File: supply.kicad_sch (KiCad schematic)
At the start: 126 parts, among them IC1 TPS54561QDPRRQ1, IC2 TPS54561QDPRRQ1, J1 BarrelJack_3167288, J2 PinHeader_1x3_P2.54mm_Drill1.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, U1 AP62301WU-7, U2 AP62301WU-7, U3 AP62301WU-7, U4 AP62301WU-7, U5 AP62301WU-7, U6 LM3881MME_NOPB

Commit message: [#65754] Rev 2.0.0 Initial commit - source design files from so-dimm-ddr5-tester e0a54f86
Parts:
- removed 1V0, 1V1, 1V8, 3V3, GND1, TP1, TP2, TP3, TP4: TP_1mm_SMD, antmicro-footprints:TP_SMD_1mm, symbol data-center-rdimm-ddr5-tester:TP_1mm_SMD
- removed C1, C2, C3, C4, C5, C6: C_47u_16V_1206, data-center-rdimm-ddr5-tester-footprints:C_1206_3216Metric, symbol data-center-rdimm-ddr5-tester:C_47u_16V_1206
- removed C10, C12: C_47p_0402, data-center-rdimm-ddr5-tester-footprints:C_0402_1005Metric, symbol data-center-rdimm-ddr5-tester:C_47p_0402
- removed C11, C9: C_10n_0402, data-center-rdimm-ddr5-tester-footprints:C_0402_1005Metric, symbol data-center-rdimm-ddr5-tester:C_10n_0402
- removed C13, C14, C26, C27, C28, C29, C30, C42: C_100n_6V3_0402, data-center-rdimm-ddr5-tester-footprints:C_0402_1005Metric, symbol data-center-rdimm-ddr5-tester:C_100n_6V3_0402
- removed C15, C16, C17, C18, C19, C20: C_47u_0603, data-center-rdimm-ddr5-tester-footprints:C_0603_1608Metric, symbol data-center-rdimm-ddr5-tester:C_47u_0603
- removed C177, C178, C179, C180, C181: C_1u_0402, data-center-rdimm-ddr5-tester-footprints:C_0402_1005Metric, symbol data-center-rdimm-ddr5-tester:C_1u_0402
- removed C21, C22, C23, C24, C25: C_10u_0402, data-center-rdimm-ddr5-tester-footprints:C_0402_1005Metric, symbol data-center-rdimm-ddr5-tester:C_10u_0402
- removed C31, C32, C33, C34, C35, C36, C37, C38, C39, C40: C_22u_0402, data-center-rdimm-ddr5-tester-footprints:C_0402_1005Metric, symbol data-center-rdimm-ddr5-tester:C_22u_0402
- removed C41: C_10n_0603, data-center-rdimm-ddr5-tester-footprints:C_0603_1608Metric, symbol data-center-rdimm-ddr5-tester:C_10n_0603
- removed C7, C8: C_4n7_0402, data-center-rdimm-ddr5-tester-footprints:C_0402_1005Metric, symbol data-center-rdimm-ddr5-tester:C_4n7_0402
- removed D1, D2, D3: PDS760, data-center-rdimm-ddr5-tester-footprints:PowerDI5, symbol data-center-rdimm-ddr5-tester:PDS760
- removed F1, F2, F3, F4, F5, F6, F7: PTC_4.5A_1206, data-center-rdimm-ddr5-tester-footprints:F_1206_3216Metric, symbol data-center-rdimm-ddr5-tester:PTC_4.5A_1206
- removed IC1, IC2: TPS54561QDPRRQ1, data-center-rdimm-ddr5-tester-footprints:WSON-10-1EP_4x4mm_P0.8mm_EP2.6x3mm, symbol data-center-rdimm-ddr5-tester:TPS54561QDPRRQ1
- removed J1: BarrelJack_3167288, data-center-rdimm-ddr5-tester-footprints:BarrelJack_3167288_Horizontal, symbol data-center-rdimm-ddr5-tester:BarrelJack_3167288
- removed J2: PinHeader_1x3_P2.54mm_Drill1.1mm, data-center-rdimm-ddr5-tester-footprints:PinHeader_1x3_P2.54mm_Drill1.1mm, symbol data-center-rdimm-ddr5-tester:PinHeader_1x3_P2.54mm_Drill1.1mm
- removed L1, L2: L_7u2_7.9A_WE-PDF, data-center-rdimm-ddr5-tester-footprints:L_WE-PDF, symbol data-center-rdimm-ddr5-tester:L_7u2_7.9A_WE-PDF
- removed L3, L5, L6, L7, L8: L_1u5_6A_1716, data-center-rdimm-ddr5-tester-footprints:L_1716_4441Metric, symbol data-center-rdimm-ddr5-tester:L_1u5_6A_1716
- removed POT1: TC33X-2-203E, data-center-rdimm-ddr5-tester-footprints:Trimpot_3.8mmx3.6mm_TC33X-2-103E, symbol data-center-rdimm-ddr5-tester:TC33X-2-203E
- removed PWR1: LED_G_0603_KP-1608CGCK, data-center-rdimm-ddr5-tester-footprints:LED_0603_1608Metric_G, symbol data-center-rdimm-ddr5-tester:LED_G_0603_KP-1608CGCK
- removed R1, R142, R16, R17, R18, R19, R20, R31: R_0R_0402, data-center-rdimm-ddr5-tester-footprints:R_0402_1005Metric, symbol data-center-rdimm-ddr5-tester:R_0R_0402
- removed R10: R_43k_0402, data-center-rdimm-ddr5-tester-footprints:R_0402_1005Metric, symbol data-center-rdimm-ddr5-tester:R_43k_0402
- removed R11, R8, R9: R_100k_0402, data-center-rdimm-ddr5-tester-footprints:R_0402_1005Metric, symbol data-center-rdimm-ddr5-tester:R_100k_0402
- removed R12, R15: R_10k2_0402, data-center-rdimm-ddr5-tester-footprints:R_0402_1005Metric, symbol data-center-rdimm-ddr5-tester:R_10k2_0402
- removed R13: R_49R9_0402, data-center-rdimm-ddr5-tester-footprints:R_0402_1005Metric, symbol data-center-rdimm-ddr5-tester:R_49R9_0402
- removed R14: R_53k6_0402, data-center-rdimm-ddr5-tester-footprints:R_0402_1005Metric, symbol data-center-rdimm-ddr5-tester:R_53k6_0402
- removed R141, R24, R28, R30, R32, R33, R34: R_10k_0402, data-center-rdimm-ddr5-tester-footprints:R_0402_1005Metric, symbol data-center-rdimm-ddr5-tester:R_10k_0402
- removed R143, R4, R5: R_243k_0402, data-center-rdimm-ddr5-tester-footprints:R_0402_1005Metric, symbol data-center-rdimm-ddr5-tester:R_243k_0402
- removed R2, R3: R_16k9_0402, data-center-rdimm-ddr5-tester-footprints:R_0402_1005Metric, symbol data-center-rdimm-ddr5-tester:R_16k9_0402
- removed R21: R_1k5_0402, data-center-rdimm-ddr5-tester-footprints:R_0402_1005Metric, symbol data-center-rdimm-ddr5-tester:R_1k5_0402
- removed R22: R_1k_0402, data-center-rdimm-ddr5-tester-footprints:R_0402_1005Metric, symbol data-center-rdimm-ddr5-tester:R_1k_0402
- removed R23: R_12k4_0402, data-center-rdimm-ddr5-tester-footprints:R_0402_1005Metric, symbol data-center-rdimm-ddr5-tester:R_12k4_0402
- removed R25: R_7k5_0402, data-center-rdimm-ddr5-tester-footprints:R_0402_1005Metric, symbol data-center-rdimm-ddr5-tester:R_7k5_0402
- removed R26: R_20k_0402, data-center-rdimm-ddr5-tester-footprints:R_0402_1005Metric, symbol data-center-rdimm-ddr5-tester:R_20k_0402
- removed R27: R_31k6_0402, data-center-rdimm-ddr5-tester-footprints:R_0402_1005Metric, symbol data-center-rdimm-ddr5-tester:R_31k6_0402
- removed R29: R_4k99_0402, data-center-rdimm-ddr5-tester-footprints:R_0402_1005Metric, symbol data-center-rdimm-ddr5-tester:R_4k99_0402
- removed R6: R_0R_2010, data-center-rdimm-ddr5-tester-footprints:R_2010_5025Metric, symbol data-center-rdimm-ddr5-tester:R_0R_2010
- removed R7: R_330R_0402, data-center-rdimm-ddr5-tester-footprints:R_0402_1005Metric, symbol data-center-rdimm-ddr5-tester:R_330R_0402
- removed S1: SW_EG1218, data-center-rdimm-ddr5-tester-footprints:SW_Slide_E-Switch_EG1218, symbol data-center-rdimm-ddr5-tester:SW_EG1218
- removed U1, U2, U3, U4, U5: AP62301WU-7, antmicro-footprints:TSOT23-6, symbol data-center-rdimm-ddr5-tester:AP62301_TSOT
- removed U6: LM3881MME_NOPB, data-center-rdimm-ddr5-tester-footprints:VSSOP-8_3x3mm_P0.65mm, symbol data-center-rdimm-ddr5-tester:LM3881
- added C169, C170, C175, C176, C195, C199, C203, C204, C205, C208, C209, C212, C214, C216, C220: C_100n_0402, antmicro-footprints:C_0402_1005Metric, symbol antmicroCapacitors0402:C_100n_0402
- added C171, C173, C177, C178, C200, C202: C_22u_25V_0805, antmicro-footprints:C_0805_2012Metric, symbol antmicroCapacitorsmisc:C_22u_25V_0805
- added C172, C174, C194, C198, C206: C_1u_0402, antmicro-footprints:C_0402_1005Metric, symbol antmicroCapacitors0402:C_1u_0402
- added C179, C180, C181: C_1u_25V_0603, antmicro-footprints:C_0603_1608Metric, symbol antmicroCapacitors0603:C_1u_25V_0603
- added C182, C183, C184, C185, C186, C187, C188, C189, C190, C191, C192, C193, C213, C215, C217, C219: C_22u_0603, antmicro-footprints:C_0603_1608Metric, symbol antmicroCapacitors0603:C_22u_0603
- added C201: C_470n_0402, antmicro-footprints:C_0402_1005Metric, symbol antmicroCapacitors0402:C_470n_0402
- added C207, C211, C218: C_10u_6.3V_0402, antmicro-footprints:C_0402_1005Metric, symbol antmicroCapacitors0402:C_10u_6.3V_0402
- added C210: C_22n_0402, antmicro-footprints:C_0402_1005Metric, symbol antmicroCapacitors0402:C_22n_0402
- added C221: C_22p_0402, antmicro-footprints:C_0402_1005Metric, symbol antmicroCapacitors0402:C_22p_0402
- added D16: ESDA25P35-1U1M, antmicro-footprints:ESDA25P35-1U1M, symbol antmicroTVSDiodes:ESDA25P35-1U1M
- added F1, F2: F_4A_1206, antmicro-footprints:F_1206_3216Metric, symbol antmicroFuses:F_4A_1206
- added J7: BarrelJack_Pin2mm_MJ-179PH, antmicro-footprints:BarrelJack_Pin2mm_MJ-179PH, symbol antmicroBarrelPowerConnectors:BarrelJack_Pin2mm_MJ-179PH
- added J8: JST_SH_1x4_BM04B-SRSS-TB-LF-SN, antmicro-footprints:Conn_JST_SH_1x4_BM04B-SRSS-TB-LF-SN, symbol antmicroWire2BoardConnectors:JST_SH_1x4_BM04B-SRSS-TB-LF-SN
- added L1: L_1u5_17A_Bourns-SRP6050CA, antmicro-footprints:L_Bourns-SRP6050CA, symbol antmicroFixedInductors:L_1u5_17A_Bourns-SRP6050CA
- added NT1, NT10, NT11, NT12, NT13, NT14, NT15, NT16, NT2, NT3, NT4, NT5, NT6, NT7, NT8, NT9: Net-Tie_P0.127mm, antmicro-footprints:NetTie-2_SMD_Pad0.127mm, symbol antmicroShuntsJumpers:Net-Tie_P0.127mm
- added Q12, Q13: SI7613DN-T1-GE3, antmicro-footprints:Vishay_PowerPAK_1212-8_Single, symbol antmicroTransistorsFETsMOSFETsSingle:SI7613DN-T1-GE3
- added Q14, Q15, Q16, Q17: BSS138PW, antmicro-footprints:SC70-3, symbol antmicroTransistorsFETsMOSFETsSingle:BSS138PW
- added R135, R139, R140, R149, R160, R161, R171, R172, R184, R187, R190: R_47k_0402, antmicro-footprints:R_0402_1005Metric, symbol antmicroResistors0402:R_47k_0402
- added R136, R137, R138, R151, R152, R153, R154, R155, R156, R157, R158, R162, R163, R164, R165, R166, R167, R168, R169: R_0R_0402, antmicro-footprints:R_0402_1005Metric, symbol antmicroResistors0402:R_0R_0402
- added R141, R142, R143, R144, R145, R146, R147, R148: R_0R01_1206, antmicro-footprints:R_1206_3216Metric, symbol antmicroResistorsmisc:R_0R01_1206
- added R170, R173, R181, R182: R_10k_0402, antmicro-footprints:R_0402_1005Metric, symbol antmicroResistors0402:R_10k_0402
- added R180: R_4k7_0402, antmicro-footprints:R_0402_1005Metric, symbol antmicroResistors0402:R_4k7_0402
- added R183, R188, R189: R_0R_22.4A_0603, antmicro-footprints:R_0603_1608Metric, symbol antmicroResistors0603:R_0R_22.4A_0603
- added R185: R_80k6_0402, antmicro-footprints:R_0402_1005Metric, symbol antmicroResistors0402:R_80k6_0402
- added R186: R_205k_0402, antmicro-footprints:R_0402_1005Metric, symbol antmicroResistors0402:R_205k_0402
- added SW4: SW_CVS-08TB, antmicro-footprints:SW_DIP_SPSTx08_Slide_Copal_CVS-08xB_W5.9mm_P1mm, symbol antmicroSlideSwitches:SW_CVS-08TB
- added SW5: SW_KMR211NGLFS_SMD, antmicro-footprints:SW_KMR211NGLFS_SMD, symbol antmicroPushbuttonSwitches:SW_KMR211NGLFS_SMD
- added TP10, TP11, TP13, TP15, TP17, TP18, TP19, TP8: TP_1mm_SMD, antmicro-footprints:TP_SMD_1mm, symbol antmicroTestPoints:TP_1mm_SMD
- added TP14, TP20, TP21: TP_1206_SMD_RCW-0C, antmicro-footprints:TP_1206_SMD_RCW-0C, symbol antmicroTestPoints:TP_1206_SMD_RCW-0C
- added U17, U18: LTC4412IS6, antmicro-footprints:SOT-23-6, symbol antmicroPMICORControllersIdealDiodes:LTC4412IS6
- added U19, U20: MPM54304GMN, antmicro-footprints:LGA-33_7x7mm_P0.65mm, symbol antmicroPMICVoltageRegulatorsDCDCSwitchingRegulators:MPM54304GMN
- added U21: NCP718BSN330T1G, antmicro-footprints:SOT-23-5, symbol antmicroPMICVoltageRegulatorsLinear:NCP718BSN330T1G
- added U22: MAX16150A_SOT, antmicro-footprints:SOT-23-6, symbol antmicroPMICPowerSequencers:MAX16150A_SOT
- added U25, U30: PAC1954T-E_VQFN, antmicro-footprints:VQFN-16-1EP_3x3mm_P0.5mm_EP1.1x1.1mm, symbol antmicroPowerMeasurement:PAC1954T-E_VQFN
- added U26: MAX812REUS+T, antmicro-footprints:SOT-143-4, symbol antmicroPMICPowerSequencers:MAX812REUS+T
- added U27: MP8869S, antmicro-footprints:MPS_QFN-14_MP8869S, symbol antmicroPMICVoltageRegulatorsDCDCSwitchingRegulators:MP8869S
- added U28: XC6230H001ER-G, antmicro-footprints:Torex_USP-6C, symbol antmicroPMICVoltageRegulatorsLinear:XC6230H001ER-G
- added U29: MCP4726A0T_DFN, antmicro-footprints:DFN-6-1EP_2x2mm_P0.65mm_EP1x1.6mm, symbol antmicroDataAcquisitionDigitaltoAnalogConvertersDAC:MCP4726A0T_DFN
- added U31: LM3880, antmicro-footprints:SOT-23-6, symbol antmicroPMICPowerSequencers:LM3880
- TP12: renamed from 5V0; symbol data-center-rdimm-ddr5-tester:TP_1mm_SMD -> antmicroTestPoints:TP_1mm_SMD
- TP16: renamed from VIN1; symbol data-center-rdimm-ddr5-tester:TP_1mm_SMD -> antmicroTestPoints:TP_1mm_SMD
- TP9: renamed from PHY1; symbol data-center-rdimm-ddr5-tester:TP_1mm_SMD -> antmicroTestPoints:TP_1mm_SMD
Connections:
- net GND: now also C169.1, C170.1, C171.1, C172.1, C173.1, C174.1, C175.1, C176.1, C177.1, C178.1, C179.1, C180.1, C181.2, C182.1, C183.1, C184.1, C185.1, C186.1, C187.1, C188.1, C189.1, C190.1, C191.1, C192.1, C193.1, C194.1, C195.1, C198.1, C199.2, C200.1, C201.1, C202.1, C203.2, C204.1, C205.1, C206.1, C207.1, C209.1, C210.1, C211.1, C212.1, C213.1, C214.2, C215.1, C216.1, C217.1, C218.1, C219.1, C220.1, D16.1 (K), J7.2, J7.3, J8.1 (Pin_1), J8.MP, Q14.2 (S), Q15.2 (S), Q16.2 (S), Q17.2 (S), R152.1, R154.1, R156.1, R158.1, R161.1, R163.1, R165.1, R167.1, R169.1, R171.1, R180.1, R186.1, SW4.13, SW4.14, SW4.17, SW4.9, SW5.1, SW5.2, TP20.1, TP21.1, U17.2 (GND), U17.3 (CTL), U18.2 (GND), U18.3 (CTL), U19.10 (GND), U19.13 (GND), U19.16 (GND), U19.17 (SGND1), U19.2 (GND), U19.20 (GND), U19.21 (GND), U19.27 (GND), U19.30 (SGND2), U19.33 (GND), U19.5 (GND), U19.7 (GND), U20.10 (GND), U20.13 (GND), U20.16 (GND), U20.17 (SGND1), U20.2 (GND), U20.20 (GND), U20.21 (GND), U20.27 (GND), U20.30 (SGND2), U20.33 (GND), U20.5 (GND), U20.7 (GND), U21.2 (GND), U22.2 (GND), U25.1 (SLOW/~{ALERT1}), U25.15 (GPIO/~{ALERT2}), U25.3 (GND), U26.1 (GND), U27.14 (AGND), U27.6 (A0), U27.8 (PGND), U28.5 (GND), U28.7 (EP), U29.5 (GND), U29.7 (SH), U30.1 (SLOW/~{ALERT1}), U30.15 (GPIO/~{ALERT2}), U30.3 (GND), U30.6 (ADDRSEL), U31.2 (GND)
- net 1V2_SYS renamed +1V2
- net +1V2: now also NT16.2, R148.2
- net VCC5V0_INT renamed +5V
- net +5V: now also C198.2, J8.2 (Pin_2), NT14.2, R146.2, R170.2
- net VIN renamed VDC
- net VDC: now also C171.2, C173.2, C177.2, C178.2, C179.2, C180.2, C181.1, C200.2, C202.2, C204.2, Q12.1 (S), Q12.2 (S), Q12.3 (S), Q13.1 (S), Q13.2 (S), Q13.3 (S), U17.6 (SENSE), U18.6 (SENSE), U19.28 (VIN), U19.29 (VIN), U20.28 (VIN), U20.29 (VIN), U21.1 (VIN), U21.3 (EN), U27.9 (VIN)
- new net: C221.1, R181.2, R185.1, R186.2
- new net: R173.2, U25.16 (~{PWRDN})
- new net: Q16.3 (D), R172.1, U26.3 (~{MR})
- new net: J8.4 (Pin_4), Q15.3 (D), R170.1
- new net: R182.2, U30.16 (~{PWRDN})
- new net: Q13.4 (G), U18.5 (GATE)
- new net: Q17.1 (G), U26.2 (~{RST})
- new net: Q12.4 (G), U17.5 (GATE)
- new net +12V: C170.2, F2.1
- new net +1V0: R188.2, R189.2, TP10.1
- new net +1V0_MGTAVCC: NT9.2, R141.2, TP8.1
- new net +1V1: C216.2, C218.2, NT15.2, R147.2, TP13.1, U29.1 (VREF)
- new net +1V2_MGTAVTT: R183.2, TP17.1
- new net +1V8: NT10.2, R142.2, TP15.1
- new net +3V3: C199.1, C205.2, C207.2, C214.1, NT13.2, R135.2, R145.2, R173.1, R182.1, TP11.1, U25.2 (VDD), U25.6 (ADDRSEL), U29.4 (VDD), U30.2 (VDD)
- new net +3V3_AON: C194.2, C195.2, C203.1, C212.2, R139.2, R140.2, R172.2, R184.2, R187.2, R190.2, TP19.1, U21.5 (VOUT), U22.3 (VCC), U26.4 (VCC), U31.1 (VCC)
- new net 12V_PCIE_fused: C176.2, F2.2, Q13.5 (D), U18.1 (IN)
- new net 12V_aux: C169.2, F1.1, J7.1
- new net 12V_aux_fused: C175.2, D16.2 (A), F1.2, Q12.5 (D), U17.1 (IN)
- new net 1V0_BS: C208.2, U27.1 (BST)
- new net 1V0_FB: R181.1, U27.11 (FB)
- new net 1V0_REG: C213.2, C215.2, C217.2, C219.2, C221.2, L1.2, R185.2, R188.1, R189.1, U27.10 (VOUT)
- new net 1V0_SS: C210.2, U27.12 (SS)
- new net 1V0_SW: C208.1, L1.1, U27.2 (SW)
- new net 1V0_VCC: C201.2, U27.13 (VCC)
- new net 1V1_SEN_+: NT7.1, U30.8 (IN3+)
- new net 1V1_SEN_-: NT15.1, U30.7 (IN3-)
- new net 1V1_local: C192.2, NT7.2, R147.1, R166.2, U20.1 (VOUT3), U20.32 (VOUT3)
- new net 1V2_SEN_+: NT8.1, U30.10 (IN4+)
- new net 1V2_SEN_-: NT16.1, U30.9 (IN4-)
- new net 1V2_local: C193.2, NT8.2, R148.1, R168.2, U20.22 (VOUT4), U20.23 (VOUT4)
- new net 1V7: C206.2, NT12.2, R144.2, TP18.1, U28.4 (EN), U28.6 (IN)
- new net 1V7_SEN_+: NT4.1, U25.10 (IN4+)
- new net 1V7_SEN_-: NT12.1, U25.9 (IN4-)
- new net 1V7_local: C189.2, NT4.2, R144.1, R164.2, U19.22 (VOUT4), U19.23 (VOUT4)
- new net 1V8_SEN_+: NT2.1, U25.13 (IN2+)
- new net 1V8_SEN_-: NT10.1, U25.14 (IN2-)
- new net 1V8_local: C183.2, C187.2, NT2.2, R142.1, R153.2, U19.8 (VOUT2), U19.9 (VOUT2)
- new net 3V3_SEN_+: NT5.1, U30.11 (IN1+)
- new net 3V3_SEN_-: NT13.1, U30.12 (IN1-)
- new net 3V3_local: C184.2, C190.2, NT5.2, R145.1, R155.2, U20.14 (VOUT1), U20.15 (VOUT1)
- new net 5V_SEN_+: NT6.1, U30.13 (IN2+)
- new net 5V_SEN_-: NT14.1, U30.14 (IN2-)
- new net 5V_local: C185.2, C191.2, NT6.2, R146.1, R157.2, U20.8 (VOUT2), U20.9 (VOUT2)
- new net DAC_VREF: C220.2, U29.6 (VOUT)
- new net EN1: R184.1, U27.5 (EN), U31.6 (FLAG1)
- new net EN2: R187.1, U19.19 (EN/SYNCI), U31.5 (FLAG2)
- new net EN3: R190.1, U20.19 (EN/SYNCI), U31.4 (FLAG3)
- new net FAN_PWM: Q15.1 (G)
- new net FB1: R151.1, R152.2, U19.18 (FB1)
- new net FB2: R153.1, R154.2, U19.6 (FB2)
- new net FB3: R162.1, R163.2, U19.31 (FB3)
- new net FB4: R164.1, R165.2, U19.24 (FB4)
- new net FB5: R155.1, R156.2, U20.18 (FB1)
- new net FB6: R157.1, R158.2, U20.6 (FB2)
- new net FB7: R166.1, R167.2, U20.31 (FB3)
- new net FB8: R168.1, R169.2, U20.24 (FB4)
- new net FPGA_POWER_CYCLE: Q16.1 (G), R171.2
- new net FPGA_POWER_OFF: Q14.1 (G), R161.2
- new net FTDI_DIS: SW4.8
- new net IN1: R139.1, SW4.3
- new net IN2: R140.1, SW4.4
- new net MGTAVCC_SEN_+: NT1.1, U25.11 (IN1+)
- new net MGTAVCC_SEN_-: NT9.1, U25.12 (IN1-)
- new net MGTAVCC_local: C182.2, C186.2, NT1.2, R141.1, R151.2, U19.14 (VOUT1), U19.15 (VOUT1)
- new net MGTAVTT_ILIM: R180.2, U28.2 (ILIM)
- new net MGTAVTT_OUT: C211.2, R183.1, U28.1 (OUT), U28.3 (FB)
- new net PB_CTRL_OUT: R149.2, R160.2, SW4.1, U22.4 (OUT)
- new net PG1: R136.2, U27.7 (PG)
- new net PG2: R137.2, U19.26 (GPIO)
- new net PG3: R138.2, U20.26 (GPIO)
- new net POWER: R135.1, R136.1, R137.1, R138.1
- new net PWR.SCL: SW4.6, SW4.7, U19.4 (SCL), U27.3 (SCL)
- new net PWR.SDA: SW4.5, U19.3 (SDA), U20.3 (SDA), U27.4 (SDA)
- new net PWR_SCL_2: SW4.11, U25.4 (SCL), U29.2 (SCL), U30.4 (SCL)
- new net PWR_SDA_2: SW4.12, U25.5 (SDA), U29.3 (SDA), U30.5 (SDA)
- new net QDCDC1_VCC: C172.2, U19.25 (VCC)
- new net QDCDC2_SCL: SW4.10, U20.4 (SCL)
- new net QDCDC2_VCC: C174.2, U20.25 (VCC)
- new net SEQ_EN: C209.2, Q17.3 (D), SW4.16, U31.3 (EN)
- new net sp_SEN_+: NT3.1, U25.8 (IN3+)
- new net sp_SEN_-: NT11.1, U25.7 (IN3-)
- new net spare: NT11.2, R143.2, TP14.1
- new net spare_local: C188.2, NT3.2, R143.1, R162.2, U19.1 (VOUT3), U19.32 (VOUT3)
- new net ~{PB_CTRL_CLR}: Q14.3 (D), R149.1, SW4.15, U22.6 (~{CLR})
- new net ~{PB_CTRL_INT}: R160.1, SW4.2, U22.5 (~{INT})
- new net ~{PB_CTRL_IN}: SW5.3, SW5.4, U22.1 (~{PB_IN})
- no-connect marks 3 -> 7
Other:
- note added: "+1V1"
- note added: "+1V2"
- note added: "+1V8"
- note added: "+3V3"
- note added: "+5V"
- note added: "1 2 3 4"
- note added: "140ms delay fixed"
- note added: "1V2 Low noise"
- note added: "7-15V"
- note added: "Always-ON +3V3 LDO"
- note added: "As both MPM54304GMN have same address (from factory), there is a need to cut SCL signals using dip switch"
- note added: "Config switch"
- note added: "DC-DC AUX, MGT"
- note added: "DC-DC INT"
- note added: "DC-DC IO"
- note added: "DC_PWR_AUX"
- note added: "FAN connector"
- note added: "Ground probe pads"
- note added: "I2C: 0x10"
- note added: "I2C: 0x1F"
- note added: "I2C: 0x60"
- note added: "I2C: 0x61"
- note added: "I2C: 0x68"
- note added: "I2C: 0x69"
- note added: "MGTAVCC"
- note added: "MGTAVTT"
- note added: "MGTAVTT Low noise LDO"
- note added: "NOTE: 1. AUTO ON/ PB-Controller 2. 8s off/ instant off 3. PWR I2C MUX input select 1 4. PWR I2C MUX input select 2 5. PWR I^{2}C SDA disconnect from 3V3 powered IC's 6. PWR I^{2}C SCL disconnect from 3V3 powered IC's 7. Connect QDCDC2 I^{2}C 8. Disable FTDI JTAG"
- note added: "NOTE: optional external divider"
- note added: "ON/OFF Button controller"
- note added: "PCIe_PWR"
- note added: "Power Monitors"
- note added: "Power cycle"
- note added: "Power good"
- note added: "Power source"
- note added: "Power supply sequencer"
- note added: "Set to ~1V7"
- note added: "Soft start delay time slot"
- note added: "VREF DAC"
- note added: "X"
- note removed: "1.0V/3A"
- note removed: "1.1V/3A"
- note removed: "1.2V/3A"
- note removed: "1.8V/3A"
- note removed: "12V DCDC BYPASS"
- note removed: "1V1 supply"
- note removed: "1V2 supply"
- note removed: "1V8 supply"
- note removed: "3V3 supply (3A)"
- note removed: "5V0 supply"
- note removed: "Fuses"
- note removed: "Input power connector"
- note removed: "Main supply (12V 5A)"
- note removed: "Optional FAN connector"
- note removed: "POT1 fine tuning: 1V1 - 0 R 1V2 - 2k5 R"
- note removed: "Power sequencer"
- note removed: "Power switch"
- note removed: "Probes"
- note removed: "STEP1 - VCCINT (1.0V) for FPGA STEP2 - VCCAUX (1.8V, 2.5V, 1.2V) for FPGA and DDR STEP3 - VCCIO (3.3V, 1.2V, 0.6V) for FPGA, PHY and DDR"
- note removed: "VCCINT (1.0V 3A)"
- title: Data Center RDIMM DDR5 Tester -> SO-DIMM DDR5 Tester

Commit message: [#65754] Rename project
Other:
- title: SO-DIMM DDR5 Tester -> RDIMM DDR5 Tester

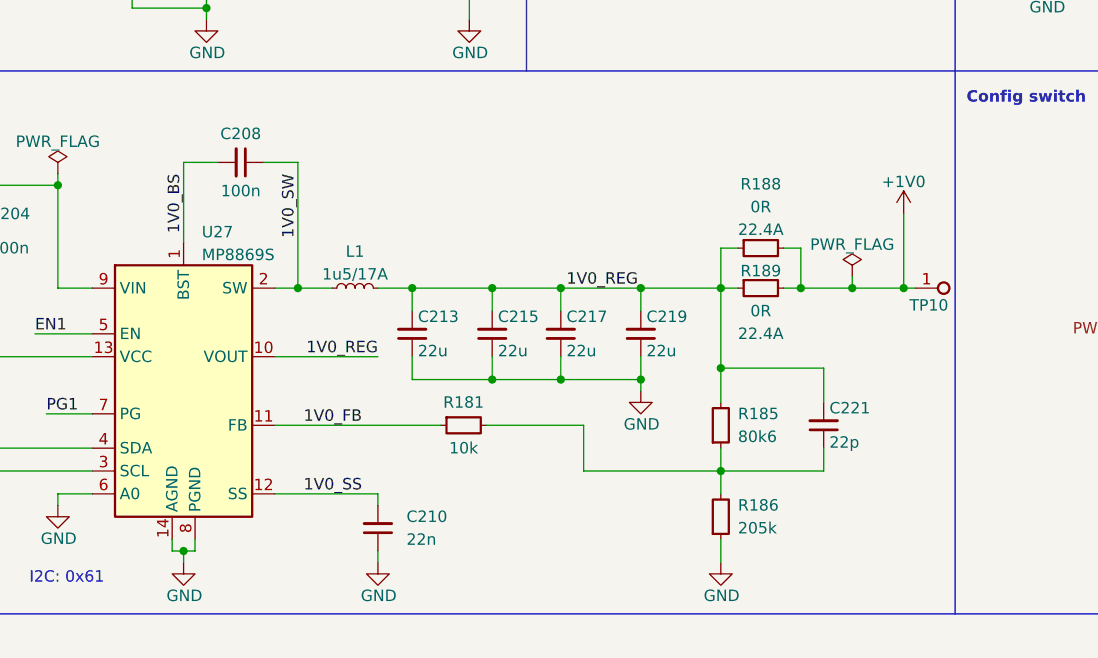
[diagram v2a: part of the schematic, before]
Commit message: [#66300] Start reconnecting power supply to support US+ voltages and power sequence
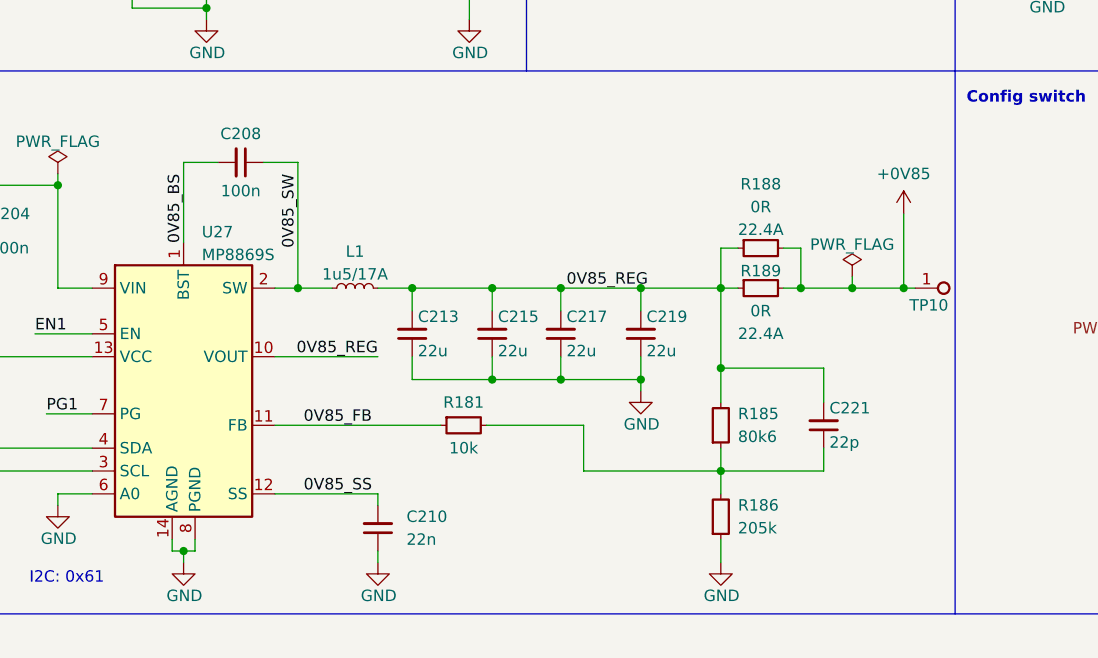
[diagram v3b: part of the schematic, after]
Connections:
- net +1V0 renamed +0V85
- net 1V0_BS renamed 0V85_BS
- net 1V0_FB renamed 0V85_FB
- net 1V0_REG renamed 0V85_REG
- net 1V0_SS renamed 0V85_SS
- net 1V0_SW renamed 0V85_SW
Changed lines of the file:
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@@
     (effects (font (size 1.27 1.27)) (justify left bottom))
   )
-  (label "1V0_REG" (at 106.68 106.68 0) (fields_autoplaced)
+  (label "0V85_REG" (at 106.68 106.68 0) (fields_autoplaced)
     (effects (font (size 1.27 1.27)) (justify left bottom))
   )
@@
     (effects (font (size 1.27 1.27)) (justify left bottom))
   )
+  (label "0V85_REG" (at 85.725 114.3 180) (fields_autoplaced)
+    (effects (font (size 1.27 1.27)) (justify right bottom))
+  )
   (label "FB8" (at 269.24 210.185 180) (fields_autoplaced)
     (effects (font (size 1.27 1.27)) (justify right bottom))
@@
     (effects (font (size 1.27 1.27)) (justify right bottom))
   )
-  (label "1V0_REG" (at 85.725 114.3 180) (fields_autoplaced)
-    (effects (font (size 1.27 1.27)) (justify right bottom))
-  )
   (label "PB_CTRL_OUT" (at 220.98 38.1 0) (fields_autoplaced)
     (effects (font (size 1.27 1.27)) (justify left bottom))
@@
     (effects (font (size 1.27 1.27)) (justify left bottom))
   )
-  (label "1V0_FB" (at 77.47 121.92 0) (fields_autoplaced)
+  (label "0V85_FB" (at 77.47 121.92 0) (fields_autoplaced)
     (effects (font (size 1.27 1.27)) (justify left bottom))
   )
@@
     (effects (font (size 1.27 1.27)) (justify right bottom))
   )
-  (label "1V0_SS" (at 77.47 129.54 0) (fields_autoplaced)
+  (label "0V85_SS" (at 77.47 129.54 0) (fields_autoplaced)
     (effects (font (size 1.27 1.27)) (justify left bottom))
   )
@@
     (effects (font (size 1.27 1.27)) (justify left bottom))
   )
-  (label "1V0_SW" (at 76.835 93.98 270) (fields_autoplaced)
+  (label "0V85_SW" (at 76.835 93.98 270) (fields_autoplaced)
     (effects (font (size 1.27 1.27)) (justify right bottom))
   )
@@
     (effects (font (size 1.27 1.27)) (justify right bottom))
   )
-  (label "1V0_BS" (at 64.135 93.98 270) (fields_autoplaced)
+  (label "0V85_BS" (at 64.135 93.98 270) (fields_autoplaced)
     (effects (font (size 1.27 1.27)) (justify right bottom))
   )
@@
     )
   )
+  (symbol (lib_id "antmicropower:+0V85") (at 144.145 98.425 0) (unit 1)
+    (in_bom yes) (on_board yes) (dnp no) (fields_autoplaced)
+    (property "Reference" "#PWR0400" (at 144.145 102.235 0)
+      (effects (font (size 1.27 1.27)) hide)
+    )
+    (property "Value" "+0V85" (at 144.145 93.98 0)
+      (effects (font (size 1.27 1.27)))
+    )
+    (property "Footprint" "" (at 144.145 98.425 0)
+      (effects (font (size 1.27 1.27)) hide)
+    )
+    (property "Datasheet" "" (at 144.145 98.425 0)
+      (effects (font (size 1.27 1.27)) hide)
+    )
+    (pin "1")
+    (instances
+      (project "data-center-rdimm-ddr5-tester"
+        (path "/1faa6543-e26a-4449-8bac-ee14b9f19e5f/00000000-0000-0000-0000-000060225b0c"
+          (reference "#PWR0400") (unit 1)
+        )
+      )
+    )
+  )
   (symbol (lib_id "antmicroResistors0402:R_0R_0402") (at 386.715 172.085 90) (unit 1)
     (in_bom yes) (on_board yes) (dnp no) (fields_autoplaced)
@@
         )
       )
-    )
-  )
-  (symbol (lib_id "antmicropower:+1V0") (at 144.145 98.425 0) (unit 1)
-    (in_bom yes) (on_board yes) (dnp no) (fields_autoplaced)
-    (property "Reference" "#PWR0397" (at 144.145 102.235 0)
-      (effects (font (size 1.27 1.27)) hide)
-    )
-    (property "Value" "+1V0" (at 144.145 94.869 0)
-      (effects (font (size 1.27 1.27)))
-    )
-    (property "Footprint" "" (at 144.145 98.425 0)
-      (effects (font (size 1.27 1.27)) hide)
-    )
-    (property "Datasheet" "" (at 144.145 98.425 0)
-      (effects (font (size 1.27 1.27)) hide)
-    )
-    (pin "1")
-    (instances
-      (project "data-center-rdimm-ddr5-tester"
-        (path "/1faa6543-e26a-4449-8bac-ee14b9f19e5f/00000000-0000-0000-0000-000060225b0c"
-          (reference "#PWR0397") (unit 1)
-        )
-      )

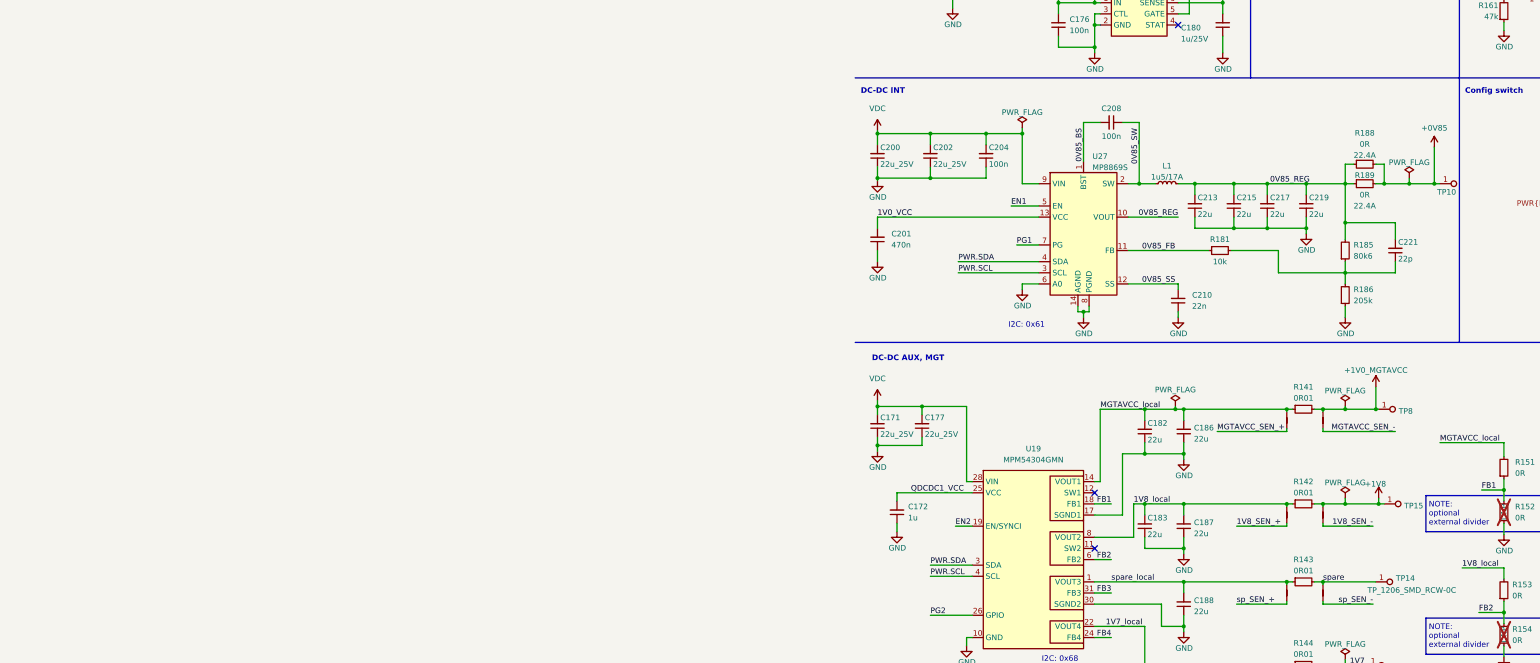
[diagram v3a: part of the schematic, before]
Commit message: [#66300] Add 30A VCCINT supply
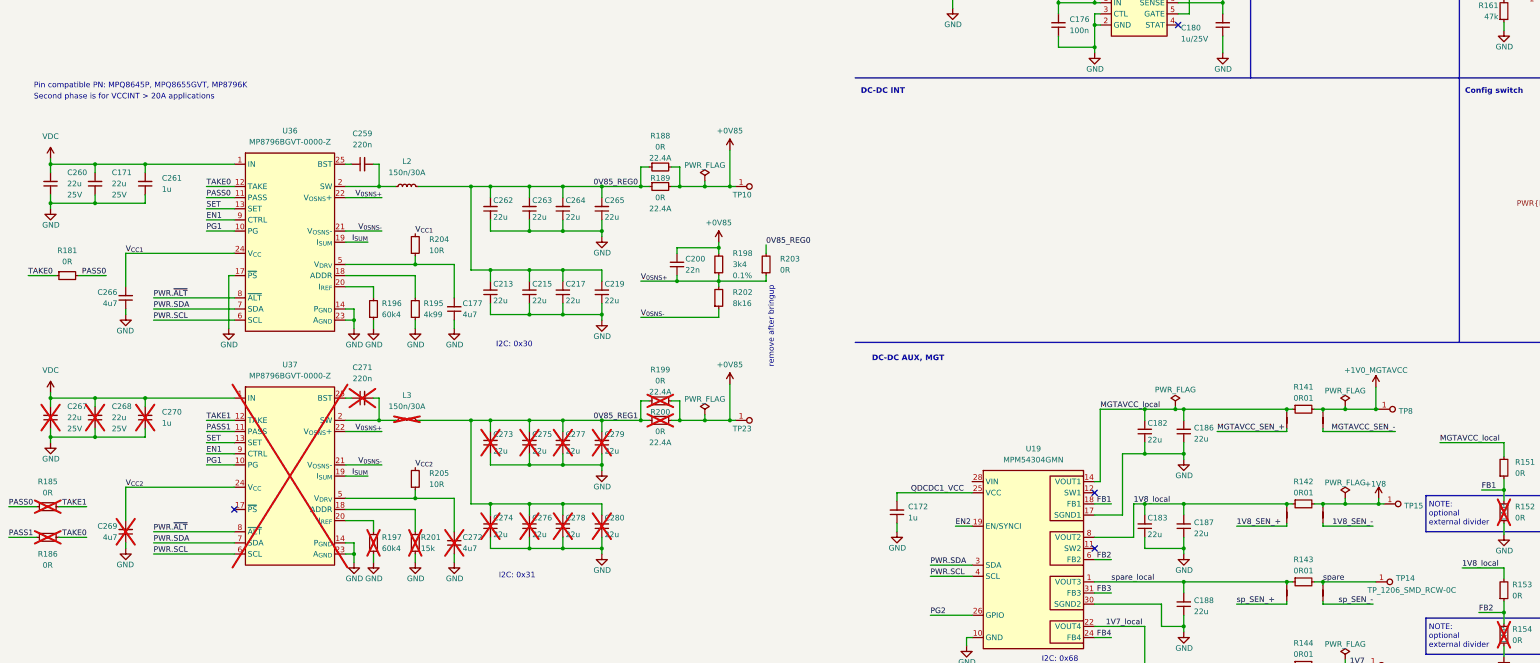
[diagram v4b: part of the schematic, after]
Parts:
- removed C177, C200, C202: C_22u_25V_0805, antmicro-footprints:C_0805_2012Metric, symbol antmicroCapacitorsmisc:C_22u_25V_0805
- removed C201: C_470n_0402, antmicro-footprints:C_0402_1005Metric, symbol antmicroCapacitors0402:C_470n_0402
- removed C204, C208: C_100n_0402, antmicro-footprints:C_0402_1005Metric, symbol antmicroCapacitors0402:C_100n_0402
- removed C210: C_22n_0402, antmicro-footprints:C_0402_1005Metric, symbol antmicroCapacitors0402:C_22n_0402
- removed C221: C_22p_0402, antmicro-footprints:C_0402_1005Metric, symbol antmicroCapacitors0402:C_22p_0402
- removed L1: L_1u5_17A_Bourns-SRP6050CA, antmicro-footprints:L_Bourns-SRP6050CA, symbol antmicroFixedInductors:L_1u5_17A_Bourns-SRP6050CA
- removed R181: R_10k_0402, antmicro-footprints:R_0402_1005Metric, symbol antmicroResistors0402:R_10k_0402
- removed R185: R_80k6_0402, antmicro-footprints:R_0402_1005Metric, symbol antmicroResistors0402:R_80k6_0402
- removed R186: R_205k_0402, antmicro-footprints:R_0402_1005Metric, symbol antmicroResistors0402:R_205k_0402
- removed U27: MP8869S, antmicro-footprints:MPS_QFN-14_MP8869S, symbol antmicroPMICVoltageRegulatorsDCDCSwitchingRegulators:MP8869S
- added C177, C266, C269, C272: C_4u7_25V_0402, antmicro-footprints:C_0402_1005Metric, symbol antmicroCapacitors0402:C_4u7_25V_0402
- added C200: C_22n_0402, antmicro-footprints:C_0402_1005Metric, symbol antmicroCapacitors0402:C_22n_0402
- added C259, C271: C_220n_16V_0402, antmicro-footprints:C_0402_1005Metric, symbol antmicroCapacitors0402:C_220n_16V_0402
- added C260, C267, C268: C_22u_25V_0805, antmicro-footprints:C_0805_2012Metric, symbol antmicroCapacitorsmisc:C_22u_25V_0805
- added C261, C270: C_1u_25V_0402, antmicro-footprints:C_0402_1005Metric, symbol antmicroCapacitors0402:C_1u_25V_0402
- added C262, C263, C264, C265, C273, C274, C275, C276, C277, C278, C279, C280: C_22u_0603, antmicro-footprints:C_0603_1608Metric, symbol antmicroCapacitors0603:C_22u_0603
- added L2, L3: L_150n_30A_WE-HCM-7050, antmicro-footprints:L_WE-HCM-7050, symbol antmicroFixedInductors:L_150n_30A_WE-HCM-7050
- added R181, R185, R186, R203: R_0R_0402, antmicro-footprints:R_0402_1005Metric, symbol antmicroResistors0402:R_0R_0402
- added R195: R_4k99_0402, antmicro-footprints:R_0402_1005Metric, symbol antmicroResistors0402:R_4k99_0402
- added R196, R197: R_60k4_0402, antmicro-footprints:R_0402_1005Metric, symbol antmicroResistors0402:R_60k4_0402
- added R198: R_3k4_0402, antmicro-footprints:R_0402_1005Metric, symbol antmicroResistors0402:R_3k4_0402
- added R199, R200: R_0R_22.4A_0603, antmicro-footprints:R_0603_1608Metric, symbol antmicroResistors0603:R_0R_22.4A_0603
- added R201: R_15k_0402, antmicro-footprints:R_0402_1005Metric, symbol antmicroResistors0402:R_15k_0402
- added R202: R_8k16_0402, antmicro-footprints:R_0402_1005Metric, symbol antmicroResistors0402:R_8k16_0402
- added R204, R205: R_10R_0402, antmicro-footprints:R_0402_1005Metric, symbol antmicroResistors0402:R_10R_0402
- added TP23: TP_1mm_SMD, antmicro-footprints:TP_SMD_1mm, symbol antmicroTestPoints:TP_1mm_SMD
- added U36, U37: MP8796B, symbol antmicroDCDCConverters:MP8796B
- C171: Dielectric (none) -> X5R; Public (none) -> False; Val 22u_25V -> 22u; Voltage (none) -> 25V
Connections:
- net +0V85: now also C200.2, R198.2, R199.2, R200.2, TP23.1
- net EN1: now also U36.9 (CTRL), U37.9 (CTRL)
- net GND: now also C177.1, C260.1, C261.1, C262.1, C263.1, C264.1, C265.1, C266.1, C267.1, C268.1, C269.1, C270.1, C272.1, C273.1, C274.1, C275.1, C276.1, C277.1, C278.1, C279.1, C280.1, R195.1, R196.1, R197.1, R201.1, U36.14 (P_{GND}), U36.15 (P_{GND}), U36.17 (~{PS}), U36.23 (A_{GND}), U36.4 (P_{GND}), U37.14 (P_{GND}), U37.15 (P_{GND}), U37.23 (A_{GND}), U37.4 (P_{GND})
- net PG1: now also U36.10 (PG), U37.10 (PG)
- net PWR.SCL: now also U36.6 (SCL), U37.6 (SCL)
- net PWR.SDA: now also U36.7 (SDA), U37.7 (SDA)
- net VDC: now also C260.2, C261.2, C267.2, C268.2, C270.2, U36.1 (IN), U36.16 (IN), U37.1 (IN), U37.16 (IN); no longer U19.28 (VIN), U19.29 (VIN)
- net 0V85_REG renamed 0V85_REG0
- net 0V85_REG0: now also C262.2, C263.2, C264.2, C265.2, L2.2, R203.2
- new net: R195.2, U36.18 (ADDR)
- new net: C259.2, L2.1, U36.2 (SW), U36.3 (SW)
- new net: R196.2, U36.20 (I_{REF})
- new net: C259.1, U36.25 (BST)
- new net: C177.2, R204.1, U36.5 (V_{DRV})
- new net: C271.2, L3.1, U37.2 (SW), U37.3 (SW)
- new net: R201.2, U37.18 (ADDR)
- new net: R197.2, U37.20 (I_{REF})
- new net: C272.2, R205.1, U37.5 (V_{DRV})
- new net: U19.28 (VIN), U19.29 (VIN)
- new net: C271.1, U37.25 (BST)
- new net 0V85_REG1: C273.2, C274.2, C275.2, C276.2, C277.2, C278.2, C279.2, C280.2, L3.2, R199.1, R200.1
- new net I_{SUM}: U36.19 (I_{SUM}), U37.19 (I_{SUM})
- new net PASS0: R181.2, R185.1, U36.11 (PASS)
- new net PASS1: R186.1, U37.11 (PASS)
- new net PWR.~{ALT}: U36.8 (~{ALT}), U37.8 (~{ALT})
- new net SET: U36.13 (SET), U37.13 (SET)
- new net TAKE0: R181.1, R186.2, U36.12 (TAKE)
- new net TAKE1: R185.2, U37.12 (TAKE)
- new net V_{0SNS+}: C200.1, R198.1, R202.2, R203.1, U36.22 (V_{OSNS}+), U37.22 (V_{OSNS}+)
- new net V_{0SNS-}: R202.1, U36.21 (V_{OSNS}-), U37.21 (V_{OSNS}-)
- new net V_{CC1}: C266.2, R204.2, U36.24 (V_{CC})
- new net V_{CC2}: C269.2, R205.2, U37.24 (V_{CC})
- no-connect marks 7 -> 8
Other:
- note added: "I2C: 0x30"
- note added: "I2C: 0x31"
- note added: "Pin compatible PN: MPQ8645P, MPQ8655GVT, MP8796K"
- note added: "Second phase is for VCCINT > 20A applications"
- note added: "remove after bringup"
- note removed: "I2C: 0x61"
- moved on the sheet: C213, C215, C217, C219, R188, R189, TP10
